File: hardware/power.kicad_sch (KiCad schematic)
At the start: 32 parts, among them U1 RY1303, U2 AP2112K-1.8, U3 AP2112K-1.8, U4 APX803-29SAG-7, U5 TPS2051BDBVR

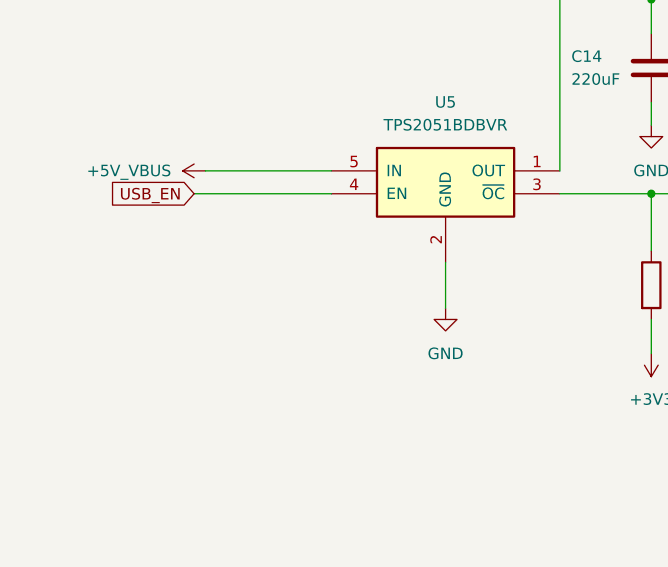
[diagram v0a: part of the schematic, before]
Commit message: 電源頁:補齊 32 個元件的 Footprint 欄位
批次修正,其中 7 個原本是錯的封裝:
  C5/C6/C7/C8  Package_SO:SOIC-8       → Capacitor_SMD:C_0603
  C9/C10       SOT-23-5                → Capacitor_SMD:C_0603
  R9           SOT-23                  → Resistor_SMD:R_0603
另 16 個原本是空的,一併填上。

依 012 §4.1 全部統一 0603,唯一例外 C14 220uF 用 SMD 電解
(Capacitor_SMD:CP_Elec_6.3x7.7,暫定,選定實際料號後要對尺寸)。

U1 RY1303 刻意留空 —— datasheet 的封裝圖是圖片,pitch/EP 尺寸未核對。
KiCad 候選 QFN-20-1EP_3x3mm_P0.4mm_EP1.65x1.65mm,
但 pitch 是 0.4 還是 0.45、EP 實際尺寸都要對原文核。已列入 011 §8 待辦。

驗證:接線與 32 個元件值均未受影響,三路 buck 回歸通過。
(改的是 property 字串,不動結構,風險低於加元件。)

另 U5 的 IN 側去耦 C16 0.1uF 已補上(使用者操作),
+5V_VBUS 現有 C2/C3/C4 10uF + C13/C16 0.1uF。

Co-Authored-By: Claude Opus 5 <noreply@anthropic.com>
Claude-Session: https://claude.ai/code/session_01HtGUWSQFey6W2g2grqgTMR
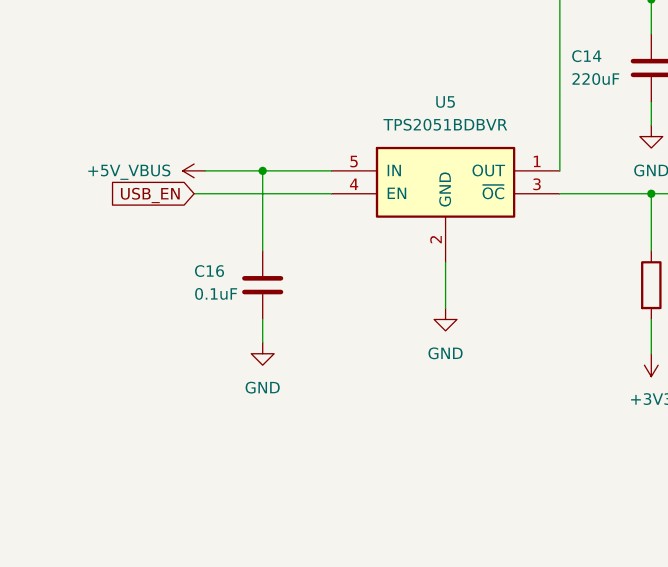
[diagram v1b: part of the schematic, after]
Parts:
- added C16: 0.1uF, Capacitor_SMD:C_0603_1608Metric, symbol Device:C
- C1, C11, C12, C15, C2, C3, C4: footprint (none) -> Capacitor_SMD:C_0603_1608Metric
- C10, C9: footprint Package_TO_SOT_SMD:SOT-23-5 -> Capacitor_SMD:C_0603_1608Metric
- C14: footprint (none) -> Capacitor_SMD:CP_Elec_6.3x7.7
- C5, C6, C7, C8: footprint Package_SO:SOIC-8_3.9x4.9mm_P1.27mm -> Capacitor_SMD:C_0603_1608Metric
- R1, R2, R3, R4, R5, R6, R7: footprint (none) -> Resistor_SMD:R_0603_1608Metric
- R9: footprint Package_TO_SOT_SMD:SOT-23 -> Resistor_SMD:R_0603_1608Metric
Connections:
- net +5V_VBUS: now also C16.1
- net GND: now also C16.2
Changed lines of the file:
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@@
 	)
 	(junction
+		(at 38.1 187.96)
+		(diameter 0)
+		(color 0 0 0 0)
+	)
+	(junction
 		(at 182.88 175.26)
 		(diameter 0)
@@
 	(wire
 		(pts
-			(xy 31.75 187.96) (xy 45.72 187.96)
+			(xy 31.75 187.96) (xy 38.1 187.96)
 		)
 		(stroke
@@
 	(wire
 		(pts
+			(xy 38.1 187.96) (xy 45.72 187.96)
+		)
+		(stroke
+			(width 0)
+			(type default)
+		)
+	)
+	(wire
+		(pts
 			(xy 365.76 121.92) (xy 374.65 121.92)
 		)
@@
 	(wire
 		(pts
+			(xy 38.1 187.96) (xy 38.1 196.85)
+		)
+		(stroke
+			(width 0)
+			(type default)
+		)
+	)
+	(wire
+		(pts
 			(xy 382.27 96.52) (xy 388.62 96.52)
 		)
@@
 		)
 	)
+	(wire
+		(pts
+			(xy 38.1 204.47) (xy 38.1 207.01)
+		)
+		(stroke
+			(width 0)
+			(type default)
+		)
+	)
 	(polyline
 		(pts
@@
 			)
 		)
-		(property "Footprint" "Package_TO_SOT_SMD:SOT-23-5"
+		(property "Footprint" "Capacitor_SMD:C_0603_1608Metric"
 			(at 28.9052 43.18 0)
 			(hide yes)
@@
 			)
 		)
-		(property "Footprint" "Package_SO:SOIC-8_3.9x4.9mm_P1.27mm"
+		(property "Footprint" "Capacitor_SMD:C_0603_1608Metric"
 			(at 382.27 106.9848 0)
 			(hide yes)
@@
 			)
 		)
-		(property "Footprint" "Package_SO:SOIC-8_3.9x4.9mm_P1.27mm"
+		(property "Footprint" "Capacitor_SMD:C_0603_1608Metric"
 			(at 382.27 133.6548 0)
 			(hide yes)
@@
 			)
 		)
-		(property "Footprint" ""
+		(property "Footprint" "Capacitor_SMD:C_0603_1608Metric"
 			(at 202.8952 194.31 0)
 			(hide yes)
@@
 			)
 		)
-		(property "Footprint" ""
+		(property "Footprint" "Resistor_SMD:R_0603_1608Metric"
 			(at 235.712 154.94 90)
 			(hide yes)
@@
 	)
 	(symbol
+		(lib_id "power:GND")
+		(at 38.1 207.01 0)
+		(unit 1)
+		(body_style 1)
+		(exclude_from_sim no)
+		(in_bom yes)
+		(on_board yes)
+		(in_pos_files yes)
+		(dnp no)
+		(fields_autoplaced yes)
+		(property "Reference" "#PWR046"
+			(at 38.1 213.36 0)
+			(hide yes)
+			(show_name no)
+			(do_not_autoplace no)
+			(effects
+				(font
+					(size 1.27 1.27)
+				)
+			)
+		)
+		(property "Value" "GND"
+			(at 38.1 212.09 0)
+			(show_name no)
+			(do_not_autoplace no)
+			(effects
+				(font
+					(size 1.27 1.27)
+				)
+			)
+		)
+		(property "Footprint" ""
+			(at 38.1 207.01 0)
+			(hide yes)
+			(show_name no)
+			(do_not_autoplace no)
+			(effects
+				(font
+					(size 1.27 1.27)
+				)
+			)
+		)
+		(property "Datasheet" ""
+			(at 38.1 207.01 0)
+			(hide yes)
+			(show_name no)
+			(do_not_autoplace no)
+			(effects
+				(font
+					(size 1.27 1.27)
+				)
+			)
+		)
+		(property "Description" "Power symbol creates a global label with name \"GND\" , ground"
+			(at 38.1 207.01 0)
+			(hide yes)
+			(show_name no)
+			(do_not_autoplace no)
+			(effects
+				(font
+					(size 1.27 1.27)
+				)
+			)
+		)
+		(pin "1"
+		)
+		(instances
+			(project "T113-DEV-V1"
+				(path "/00000000-0000-0000-0000-000000000001/04570e9e-060d-4156-8a20-e24c8ec7616f"
+					(reference "#PWR046")
+					(unit 1)
+				)
+			)
+		)
+	)
+	(symbol
 		(lib_id "power:+3V3")
 		(at 308.61 201.93 270)
@@
 			)
 		)
-		(property "Footprint" ""
+		(property "Footprint" "Capacitor_SMD:C_0603_1608Metric"
 			(at 93.6752 180.34 0)
 			(hide yes)
@@
 			)
 		)
-		(property "Footprint" "Package_TO_SOT_SMD:SOT-23"
+		(property "Footprint" "Resistor_SMD:R_0603_1608Metric"
 			(at 79.502 200.66 90)
 			(hide yes)
@@
 			)
 		)
-		(property "Footprint" ""
+		(property "Footprint" "Capacitor_SMD:C_0603_1608Metric"
 			(at 213.0552 194.31 0)
 			(hide yes)
@@
 			)
 		)
-		(property "Footprint" ""
+		(property "Footprint" "Capacitor_SMD:C_0603_1608Metric"
 			(at 192.7352 194.31 0)
 			(hide yes)
@@
 			)
 		)
-		(property "Footprint" ""
+		(property "Footprint" "Resistor_SMD:R_0603_1608Metric"
 			(at 336.042 203.2 90)
 			(hide yes)
@@
 			)
 		)
-		(property "Footprint" ""
+		(property "Footprint" "Resistor_SMD:R_0603_1608Metric"
 			(at 351.79 192.532 90)
 			(hide yes)
@@
 			)
 		)
-		(property "Footprint" "Package_SO:SOIC-8_3.9x4.9mm_P1.27mm"
+		(property "Footprint" "Capacitor_SMD:C_0603_1608Metric"
 			(at 382.27 95.5548 0)
 			(hide yes)
@@
 			)
 		)
-		(property "Footprint" ""
+		(property "Footprint" "Resistor_SMD:R_0603_1608Metric"
 			(at 387.35 192.532 90)
 			(hide yes)
@@
 			)
 		)
-		(property "Footprint" "Package_TO_SOT_SMD:SOT-23-5"
+		(property "Footprint" "Capacitor_SMD:C_0603_1608Metric"
 			(at 30.1752 91.44 0)
 			(hide yes)
@@
 			)
 		)
-		(property "Footprint" ""
+		(property "Footprint" "Capacitor_SMD:C_0603_1608Metric"
 			(at 83.5152 91.44 0)
 			(hide yes)
@@
 	)
 	(symbol
+		(lib_id "Device:C")
+		(at 38.1 200.66 0)
+		(unit 1)
+		(body_style 1)
+		(exclude_from_sim no)
+		(in_bom yes)
+		(on_board yes)
+		(in_pos_files yes)
+		(dnp no)
+		(property "Reference" "C16"
+			(at 30.48 199.136 0)
+			(show_name no)
+			(do_not_autoplace no)
+			(effects
+				(font
+					(size 1.27 1.27)
+				)
+				(justify left)
+			)
+		)
+		(property "Value" "0.1uF"
+			(at 30.48 201.676 0)
+			(show_name no)
+			(do_not_autoplace no)
+			(effects
+				(font
+					(size 1.27 1.27)
+				)
+				(justify left)
+			)
+		)
+		(property "Footprint" "Capacitor_SMD:C_0603_1608Metric"
+			(at 39.0652 204.47 0)
+			(hide yes)
+			(show_name no)
+			(do_not_autoplace no)
+			(effects
+				(font
+					(size 1.27 1.27)
+				)
+			)
+		)
+		(property "Datasheet" ""
+			(at 38.1 200.66 0)
+			(hide yes)
+			(show_name no)
+			(do_not_autoplace no)
+			(effects
+				(font
+					(size 1.27 1.27)
+				)
+			)
+		)
+		(property "Description" "Unpolarized capacitor"
+			(at 38.1 200.66 0)
+			(hide yes)
+			(show_name no)
+			(do_not_autoplace no)
+			(effects
+				(font
+					(size 1.27 1.27)
+				)
+			)
+		)
+		(pin "2"
+		)
+		(pin "1"
+		)
+		(instances
+			(project "T113-DEV-V1"
+				(path "/00000000-0000-0000-0000-000000000001/04570e9e-060d-4156-8a20-e24c8ec7616f"
+					(reference "C16")
+					(unit 1)
+				)
+			)
+		)
+	)
+	(symbol
 		(lib_id "Device:L")
 		(at 312.42 175.26 90)
@@
 			)
 		)
-		(property "Footprint" "Package_SO:SOIC-8_3.9x4.9mm_P1.27mm"
+		(property "Footprint" "Capacitor_SMD:C_0603_1608Metric"
 			(at 382.27 120.9548 0)
 			(hide yes)
@@
 			)
 		)
-		(property "Footprint" ""
+		(property "Footprint" "Resistor_SMD:R_0603_1608Metric"
 			(at 302.26 200.152 90)
 			(hide yes)
@@
 			)
 		)
-		(property "Footprint" ""
+		(property "Footprint" "Resistor_SMD:R_0603_1608Metric"
 			(at 371.602 203.2 90)
 			(hide yes)
@@
 			)
 		)
-		(property "Footprint" ""
+		(property "Footprint" "Resistor_SMD:R_0603_1608Metric"
 			(at 286.512 210.82 90)
 			(hide yes)
@@
 			)
 		)
-		(property "Footprint" ""
+		(property "Footprint" "Capacitor_SMD:C_0603_1608Metric"
 			(at 80.9752 43.18 0)
 			(hide yes)
@@
 			)
 		)
-		(property "Footprint" ""
+		(property "Footprint" "Capacitor_SMD:CP_Elec_6.3x7.7"
 			(at 82.2452 180.34 0)
 			(hide yes)
@@
 			)
 		)
-		(property "Footprint" ""
+		(property "Footprint" "Capacitor_SMD:C_0603_1608Metric"
 			(at 221.9452 161.29 0)
 			(hide yes)

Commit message: 修正 C5~C8 的封裝為 0805;012 補記兩個 0603 例外
C5/C6/C7/C8 是 RY1303 三路 buck 的 22uF 輸出電容,
011 §2.4 定的料號 C45783 是 0805 X5R —— 前一個 commit 批次填成 0603 是錯的。
22uF 在 0603 的 DC bias 衰減太嚴重(概念 ⑧),所以當初才選 0805。

012 §4.1.1 從「唯一的例外」改成「兩個例外」:
  ① C5~C8 22uF 用 0805(DC bias)
  ② C14 220uF SMD 電解(USB 2.0 規範的 120uF bulk 要求)
並附電源頁完成時的封裝分布,方便日後核對。

驗證:三路 buck 回歸通過,接線與值未受影響。

Co-Authored-By: Claude Opus 5 <noreply@anthropic.com>
Claude-Session: https://claude.ai/code/session_01HtGUWSQFey6W2g2grqgTMR
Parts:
- C5, C6, C7, C8: footprint Capacitor_SMD:C_0603_1608Metric -> Capacitor_SMD:C_0805_2012Metric
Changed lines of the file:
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@@
 			)
 		)
-		(property "Footprint" "Capacitor_SMD:C_0603_1608Metric"
+		(property "Footprint" "Capacitor_SMD:C_0805_2012Metric"
 			(at 382.27 106.9848 0)
 			(hide yes)
@@
 			)
 		)
-		(property "Footprint" "Capacitor_SMD:C_0603_1608Metric"
+		(property "Footprint" "Capacitor_SMD:C_0805_2012Metric"
 			(at 382.27 133.6548 0)
 			(hide yes)
@@
 			)
 		)
-		(property "Footprint" "Capacitor_SMD:C_0603_1608Metric"
+		(property "Footprint" "Capacitor_SMD:C_0805_2012Metric"
 			(at 382.27 95.5548 0)
 			(hide yes)
@@
 			)
 		)
-		(property "Footprint" "Capacitor_SMD:C_0603_1608Metric"
+		(property "Footprint" "Capacitor_SMD:C_0805_2012Metric"
 			(at 382.27 120.9548 0)
 			(hide yes)

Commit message: 佈線前置總驗收通過;修掉根圖紙上四張子頁蓋住 Main Chip 的問題
這一輪做了四項之前沒驗過的檢查,抓到一個排版問題。

★ 根圖紙上「Main Chip」被四張新子頁蓋住
   new_sheet.py 原本用「第 n 張放第 n 格」算位置,但電源與 Main Chip
   是手動放的,位置不在格線上,而且 Main Chip 比標準格子大(100x71mm)。
   結果 MIPI/網路/排針/音訊四張疊在它上面 —— 電氣沒影響,
   但根圖紙上點不到被蓋住的方塊,很難用。
   改成:讀出既有所有方塊的矩形,逐一試候選位置,挑第一個不重疊的。
   順手修掉 SLOTS 自己的 bug(236.22+88.9 > 320.04,第二三格會互撞)。

其餘三項新檢查都過
   BOM 匯出 209 列,DNP 標記正確(R65/R68/R78 = strap 不焊的那三顆)
   跨頁 UUID 3830 個,重複 0
   page 編號無重複

佈線前置總驗收(真實專案,從乾淨狀態完整重跑 27 步)
   ① ERC                0 errors · 0 warnings
   ② check_schematic    0 errors · 0 warnings
   ③ check_power_rails  全部通過
   ④ check_footprints   209 顆元件腳號全部對得上焊盤
   ⑤ BOM 匯出           209 列
   ⑥ 根圖紙             10 張子頁,方塊重疊 0
   ⑦ 元素 UUID          3830 個,重複 0
   ⑧ netclass           六類分組就位(線寬待 JLCPCB 阻抗回算)

可以 Update PCB from Schematic 了。

Co-Authored-By: Claude Opus 5 <noreply@anthropic.com>
Claude-Session: https://claude.ai/code/session_01HtGUWSQFey6W2g2grqgTMR
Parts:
- U1: footprint (none) -> Package_DFN_QFN:UQFN-20-1EP_3x3mm_P0.4mm_EP1.7x1.7mm_ThermalVias
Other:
- note added: "PWR_FLAG —— 給 ERC 看的，不是真元件"
- note added: "⚠ 只能用在確實有電的地方 —— 拿它蓋掉真的沒接的軌等於把安全網剪掉。"
- note added: "所以 ERC 在輸出節點上找不到任何 power_out 腳，判定「沒人驅動」。"
- note added: "降壓器的輸出走 SW 腳 ->[電感]-> 輸出節點，電感是被動件，"
